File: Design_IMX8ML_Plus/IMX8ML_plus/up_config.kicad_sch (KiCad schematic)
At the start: 6 parts, among them U1 MIMX8ML8CVNKZAB, U6 KSZ9131RNXI, Y2 24MHz

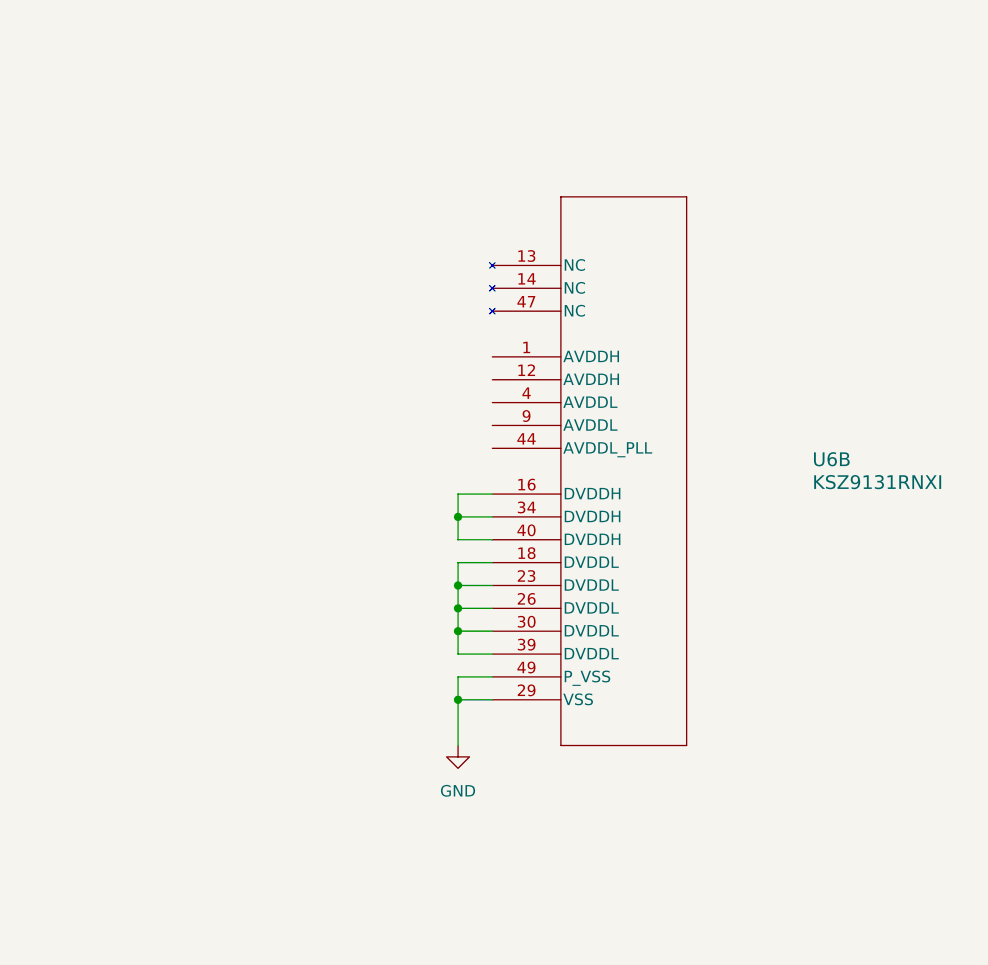
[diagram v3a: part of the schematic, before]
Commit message: reorganization of the componentes
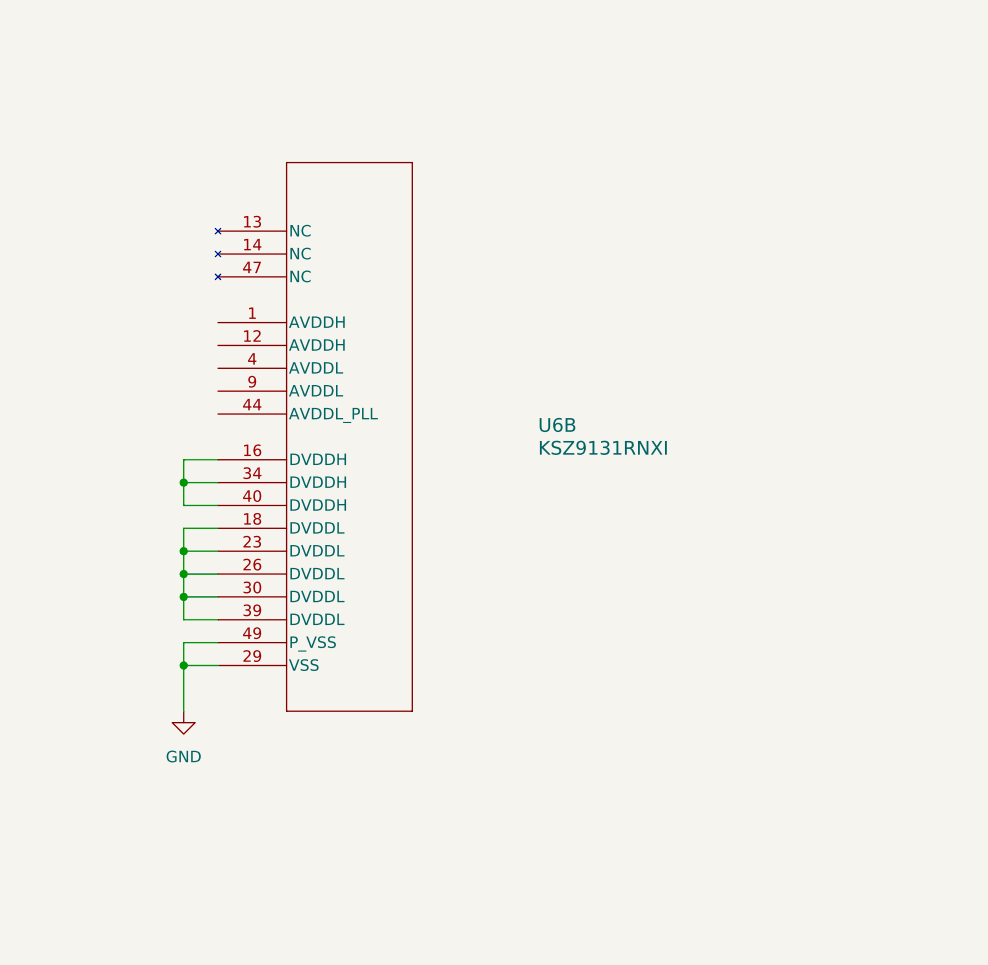
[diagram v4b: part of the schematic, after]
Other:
- moved on the sheet: U6B
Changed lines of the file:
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@@
 	(paper "A4")
 	(junction
-		(at 251.46 134.62)
+		(at 220.98 130.81)
 		(diameter 0)
 		(color 0 0 0 0)
@@
 	)
 	(junction
-		(at 251.46 147.32)
+		(at 220.98 143.51)
 		(diameter 0)
 		(color 0 0 0 0)
 	)
 	(junction
-		(at 251.46 144.78)
+		(at 220.98 140.97)
 		(diameter 0)
 		(color 0 0 0 0)
 	)
 	(junction
-		(at 251.46 154.94)
+		(at 220.98 151.13)
 		(diameter 0)
 		(color 0 0 0 0)
@@
 	)
 	(junction
-		(at 251.46 142.24)
+		(at 220.98 138.43)
 		(diameter 0)
 		(color 0 0 0 0)
@@
 	(wire
 		(pts
-			(xy 251.46 147.32) (xy 251.46 149.86)
+			(xy 220.98 143.51) (xy 220.98 146.05)
 		)
 		(stroke
@@
 	(wire
 		(pts
-			(xy 255.27 139.7) (xy 251.46 139.7)
+			(xy 224.79 135.89) (xy 220.98 135.89)
 		)
 		(stroke
@@
 	(wire
 		(pts
-			(xy 251.46 144.78) (xy 255.27 144.78)
+			(xy 220.98 140.97) (xy 224.79 140.97)
 		)
 		(stroke
@@
 	(wire
 		(pts
-			(xy 251.46 147.32) (xy 255.27 147.32)
+			(xy 220.98 143.51) (xy 224.79 143.51)
 		)
 		(stroke
@@
 	(wire
 		(pts
-			(xy 255.27 152.4) (xy 251.46 152.4)
+			(xy 224.79 148.59) (xy 220.98 148.59)
 		)
 		(stroke
@@
 	(wire
 		(pts
-			(xy 251.46 154.94) (xy 255.27 154.94)
+			(xy 220.98 151.13) (xy 224.79 151.13)
 		)
 		(stroke
@@
 	(wire
 		(pts
-			(xy 251.46 132.08) (xy 255.27 132.08)
+			(xy 220.98 128.27) (xy 224.79 128.27)
 		)
 		(stroke
@@
 	(wire
 		(pts
-			(xy 251.46 134.62) (xy 255.27 134.62)
+			(xy 220.98 130.81) (xy 224.79 130.81)
 		)
 		(stroke
@@
 	(wire
 		(pts
-			(xy 251.46 142.24) (xy 255.27 142.24)
+			(xy 220.98 138.43) (xy 224.79 138.43)
 		)
 		(stroke
@@
 	(wire
 		(pts
-			(xy 251.46 154.94) (xy 251.46 160.02)
+			(xy 220.98 151.13) (xy 220.98 156.21)
 		)
 		(stroke
@@
 	(wire
 		(pts
-			(xy 255.27 137.16) (xy 251.46 137.16)
+			(xy 224.79 133.35) (xy 220.98 133.35)
 		)
 		(stroke
@@
 	(wire
 		(pts
-			(xy 251.46 149.86) (xy 255.27 149.86)
+			(xy 220.98 146.05) (xy 224.79 146.05)
 		)
 		(stroke
@@
 	(wire
 		(pts
-			(xy 251.46 152.4) (xy 251.46 154.94)
+			(xy 220.98 148.59) (xy 220.98 151.13)
 		)
 		(stroke
@@
 	(wire
 		(pts
-			(xy 251.46 134.62) (xy 251.46 132.08)
+			(xy 220.98 130.81) (xy 220.98 128.27)
 		)
 		(stroke
@@
 	(wire
 		(pts
-			(xy 251.46 142.24) (xy 251.46 144.78)
+			(xy 220.98 138.43) (xy 220.98 140.97)
 		)
 		(stroke
@@
 	(wire
 		(pts
-			(xy 251.46 137.16) (xy 251.46 134.62)
+			(xy 220.98 133.35) (xy 220.98 130.81)
 		)
 		(stroke
@@
 	(wire
 		(pts
-			(xy 251.46 144.78) (xy 251.46 147.32)
+			(xy 220.98 140.97) (xy 220.98 143.51)
 		)
 		(stroke
@@
 	(wire
 		(pts
-			(xy 251.46 139.7) (xy 251.46 142.24)
+			(xy 220.98 135.89) (xy 220.98 138.43)
 		)
 		(stroke
@@
 	(symbol
 		(lib_id "KSZ9131RNXI:KSZ9131RNXI")
-		(at 255.27 106.68 0)
+		(at 224.79 102.87 0)
 		(unit 2)
 		(exclude_from_sim no)
@@
 		(fields_autoplaced yes)
 		(property "Reference" "U6"
-			(at 290.83 128.27 0)
+			(at 260.35 124.46 0)
 			(effects
 				(font
@@
 		)
 		(property "Value" "KSZ9131RNXI"
-			(at 290.83 130.81 0)
+			(at 260.35 127 0)
 			(effects
 				(font
@@
 		)
 		(property "Footprint" "Package_DFN_QFN:QFN-48-1EP_7x7mm_P0.5mm_EP5.6x5.6mm"
-			(at 255.27 106.68 0)
+			(at 224.79 102.87 0)
 			(effects
 				(font
@@
 		)
 		(property "Datasheet" "KSZ9131RNXI"
-			(at 255.27 106.68 0)
+			(at 224.79 102.87 0)
 			(effects
 				(font
@@
 		)
 		(property "Description" ""
-			(at 255.27 106.68 0)
+			(at 224.79 102.87 0)
 			(effects
 				(font
@@
 	(symbol
 		(lib_id "power:GND")
-		(at 251.46 160.02 0)
+		(at 220.98 156.21 0)
 		(unit 1)
 		(exclude_from_sim no)
@@
 		(fields_autoplaced yes)
 		(property "Reference" "#PWR05"
-			(at 251.46 166.37 0)
+			(at 220.98 162.56 0)
 			(effects
 				(font
@@
 		)
 		(property "Value" "GND"
-			(at 251.46 165.1 0)
+			(at 220.98 161.29 0)
 			(effects
 				(font
@@
 		)
 		(property "Footprint" ""
-			(at 251.46 160.02 0)
+			(at 220.98 156.21 0)
 			(effects
 				(font
@@
 		)
 		(property "Datasheet" ""
-			(at 251.46 160.02 0)
+			(at 220.98 156.21 0)
 			(effects
 				(font
@@
 		)
 		(property "Description" ""
-			(at 251.46 160.02 0)
+			(at 220.98 156.21 0)
 			(effects
 				(font

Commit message: CPU Board actualizate
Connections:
- net USB2_DNU: now reaches U1.E12 (USB2_DNU)
- net USB2_TXRTUNE: now reaches U1.F12 (USB2_TXRTUNE)
- no-connect marks 1 -> 0
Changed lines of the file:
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@@
 		(color 0 0 0 0)
 	)
-	(no_connect
-		(at 99.06 30.48)
+	(wire
+		(pts
+			(xy 99.06 43.18) (xy 107.95 43.18)
+		)
+		(stroke
+			(width 0)
+			(type default)
+		)
 	)
 	(wire
@@
 	(wire
 		(pts
+			(xy 99.06 30.48) (xy 107.95 30.48)
+		)
+		(stroke
+			(width 0)
+			(type default)
+		)
+	)
+	(wire
+		(pts
 			(xy 135.89 134.62) (xy 144.78 134.62)
 		)
@@
 		)
 	)
+	(global_label "USB2_TXRTUNE"
+		(shape input)
+		(at 107.95 43.18 0)
+		(fields_autoplaced yes)
+		(effects
+			(font
+				(size 1 1)
+			)
+			(justify left)
+		)
+		(property "Intersheetrefs" "${INTERSHEET_REFS}"
+			(at 121.4908 43.18 0)
+			(effects
+				(font
+					(size 1.27 1.27)
+				)
+				(justify left)
+				(hide yes)
+			)
+		)
+	)
 	(global_label "ENET_RD2"
 		(shape input)
@@
 				(hide yes)
 			)
+		)
+	)
+	(global_label "USB2_DNU"
+		(shape input)
+		(at 107.95 30.48 0)
+		(fields_autoplaced yes)
+		(effects
+			(font
+				(size 1 1)
+			)
+			(justify left)
+		)
+		(property "Intersheetrefs" "${INTERSHEET_REFS}"
+			(at 118.1098 30.48 0)
+			(effects
+				(font
+					(size 1.27 1.27)
+				)
+				(justify left)
+				(hide yes)
+			)

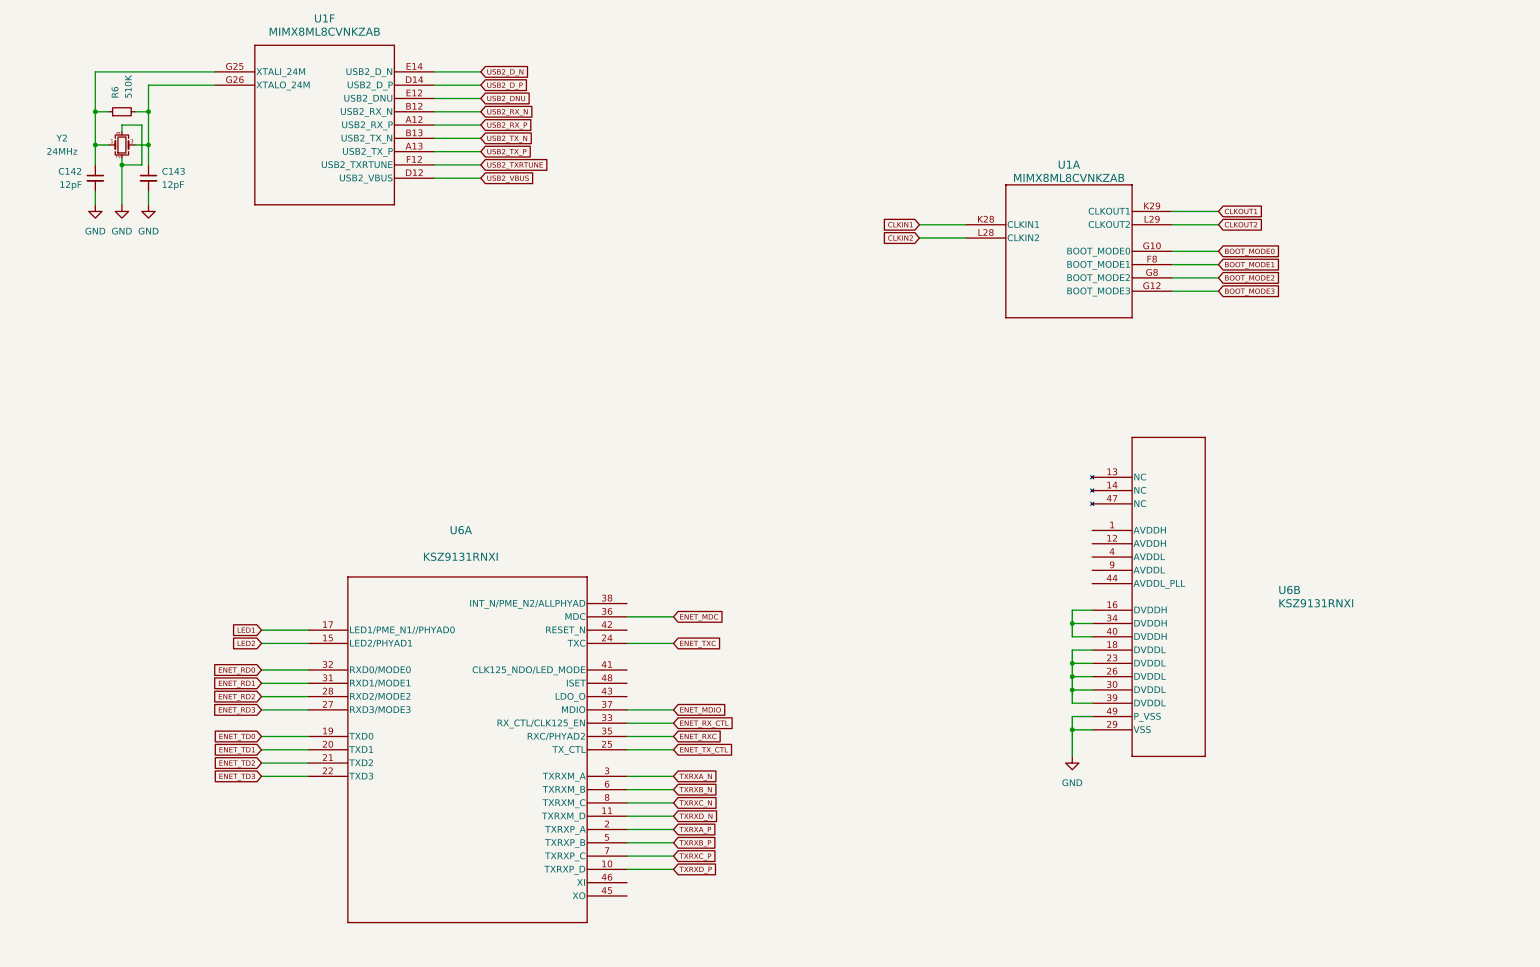
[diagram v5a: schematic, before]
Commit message: [PROCESSOR] Create zones It added power zones in the four layer
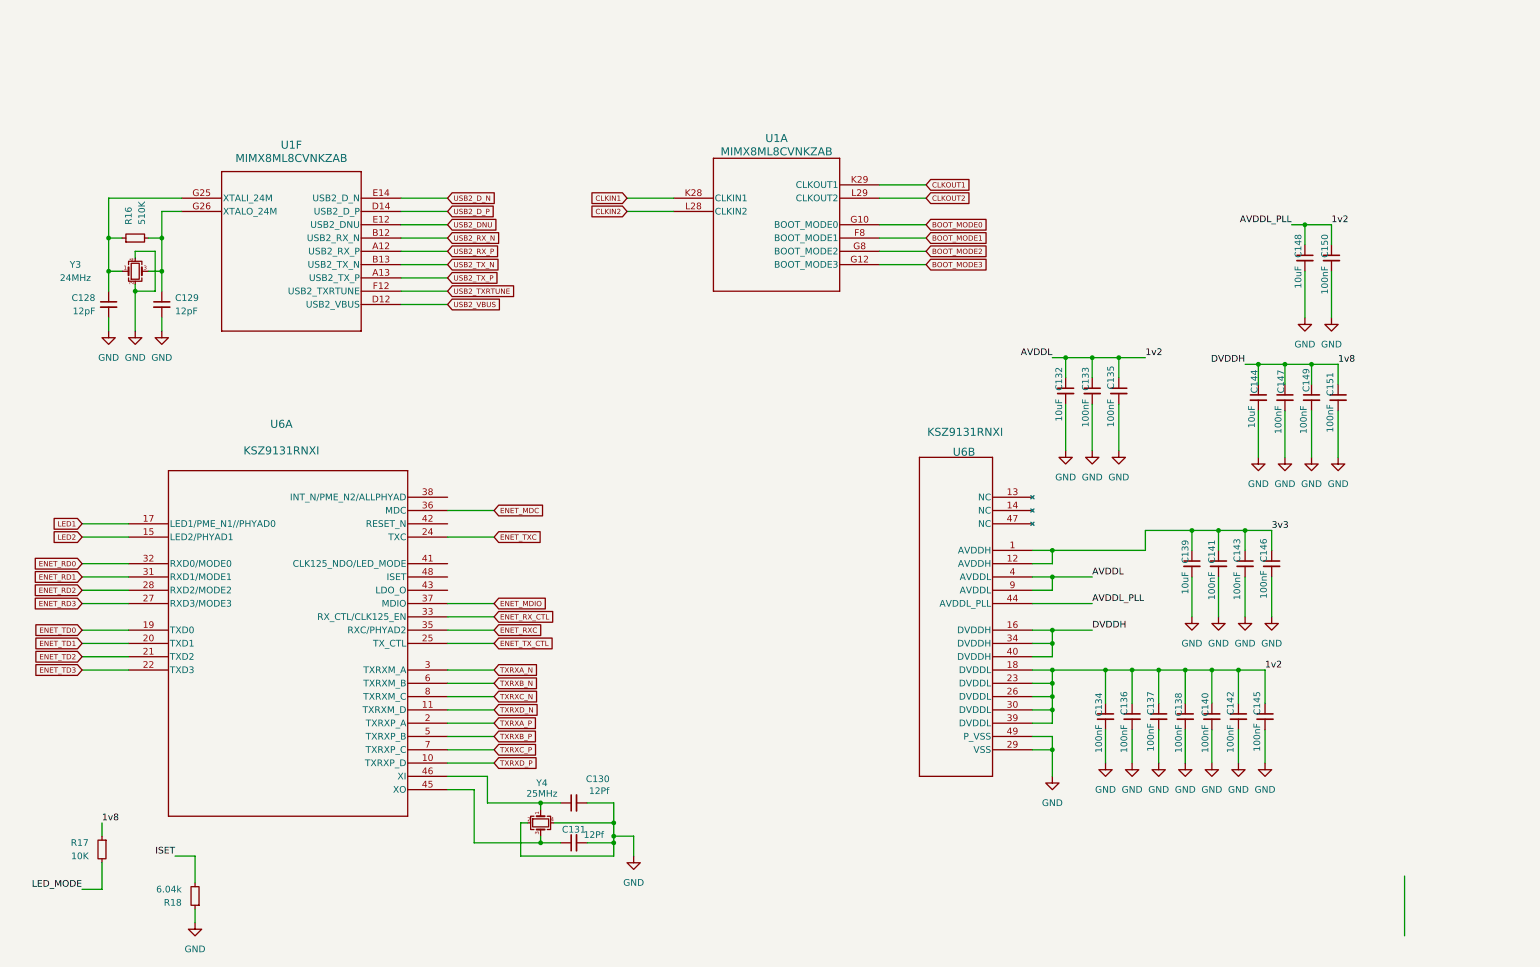
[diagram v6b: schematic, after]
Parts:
- added C130, C131: 12Pf, Capacitor_SMD:C_0402_1005Metric, symbol Device:C_Small
- added C132, C139, C144, C148: 10uF, Capacitor_SMD:C_0402_1005Metric, symbol Device:C_Small
- added C133, C134, C135, C136, C137, C138, C140, C141, C142, C143, C145, C146, C147, C149, C150, C151: 100nF, Capacitor_SMD:C_0402_1005Metric, symbol Device:C_Small
- added R17: 10K, Resistor_SMD:R_0402_1005Metric, symbol Device:R_Small
- added R18: 6.04k, Resistor_SMD:R_0402_1005Metric, symbol Device:R_Small
- added Y4: 25MHz, Crystal:Crystal_SMD_0603-4Pin_6.0x3.5mm, symbol Device:Crystal_GND24_Small
- renumbered C142 to C128, C143 to C129, R6 to R16, Y2 to Y3
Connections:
- net GND: now also C130.2, C131.2, C132.2, C133.2, C134.2, C135.2, C136.2, C137.2, C138.2, C139.2, C140.2, C141.2, C142.2, C143.2, C144.2, C145.2, C146.2, C147.2, C148.2, C149.2, C150.2, C151.2, R18.1, Y4.2, Y4.4
- net 3v3: now reaches U6.1 (AVDDH)
- net 3v3: now also U6.12 (AVDDH), C139.1, C141.1, C143.1, C146.1
- net 1v8: now reaches U6.16 (DVDDH), U6.34 (DVDDH), U6.40 (DVDDH)
- net 1v8: now also C144.1, C147.1, C149.1, C151.1, R17.1
- net 1v2: now reaches U6.18 (DVDDL), U6.23 (DVDDL), U6.26 (DVDDL), U6.30 (DVDDL), U6.39 (DVDDL)
- net 1v2: now also U6.4 (AVDDL), U6.44 (AVDDL_PLL), U6.9 (AVDDL), C132.1, C133.1, C134.1, C135.1, C136.1, C137.1, C138.1, C140.1, C142.1, C145.1, C148.1, C150.1
- net at U6.45 (XO): now also C131.1, Y4.3
- net at U6.46 (XI): now also C130.1, Y4.1
- new net ISET: R18.2
- new net LED_MODE: R17.2
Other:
- moved on the sheet: C128, C129, R16, U1A, U1F, U6A, U6B, Y3

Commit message: [IMX8ML-CPU] LPDDR4 memories reorganization of track between processor and memories.
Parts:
- Y4: footprint Crystal:Crystal_SMD_0603-4Pin_6.0x3.5mm -> Crystal:Crystal_SMD_3225-4Pin_3.2x2.5mm
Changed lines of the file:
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@@
 			)
 		)
-		(property "Footprint" "Crystal:Crystal_SMD_0603-4Pin_6.0x3.5mm"
+		(property "Footprint" "Crystal:Crystal_SMD_3225-4Pin_3.2x2.5mm"
 			(at 119.38 168.91 0)
 			(effects
